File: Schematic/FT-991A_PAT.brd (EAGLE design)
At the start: 44.6 x 59.8 mm, 50 parts, among them Q10 PE4259, Q2 MC78L09ABDR2GOSCT, Q3 SN74AHC-OR, Q4 PE4259, Q5 NCP553, Q6 PE4259, Q7 J310, Q8 5086, Q9 PE4259, X1 IF_IN, X2 SCP_OUT, X3 SDR_OUT

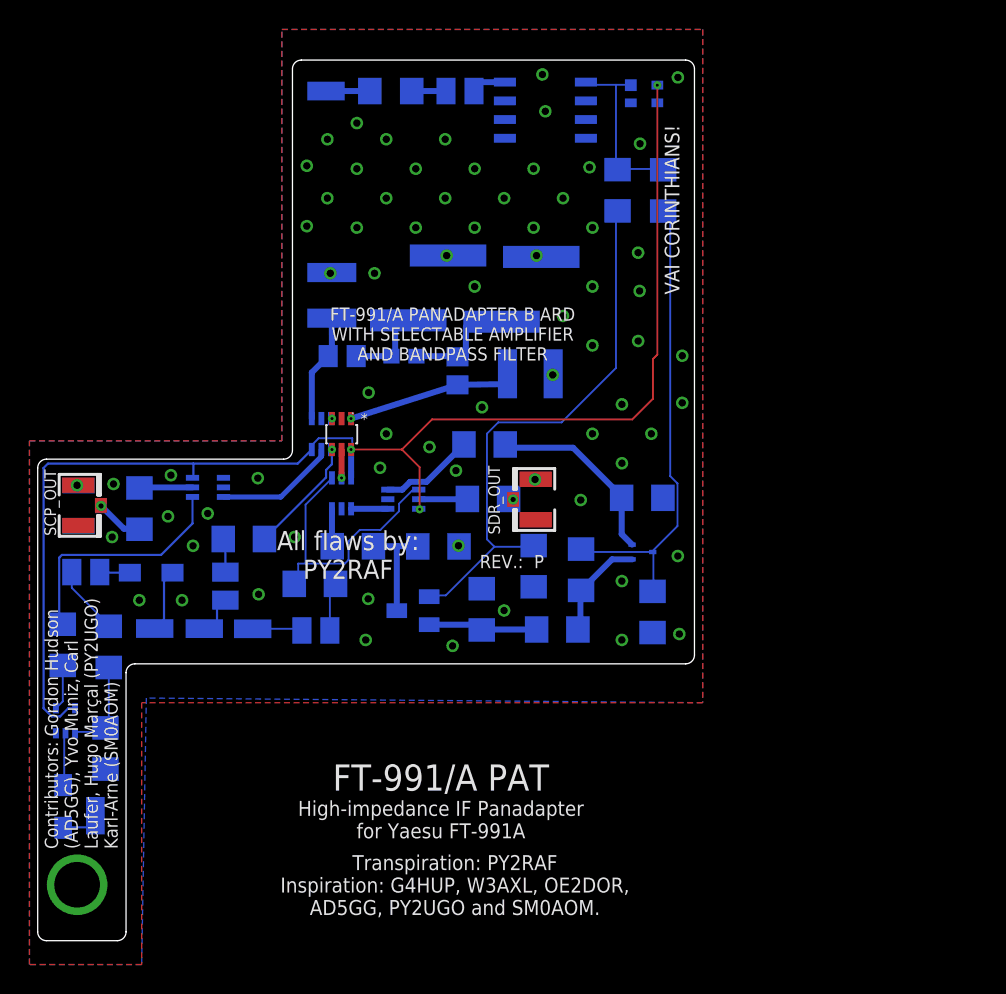
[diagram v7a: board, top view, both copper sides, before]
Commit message: Added test points
Added test points for voltage and RF switch lines.
Updated board, schematics and gerbers to reflect the change.
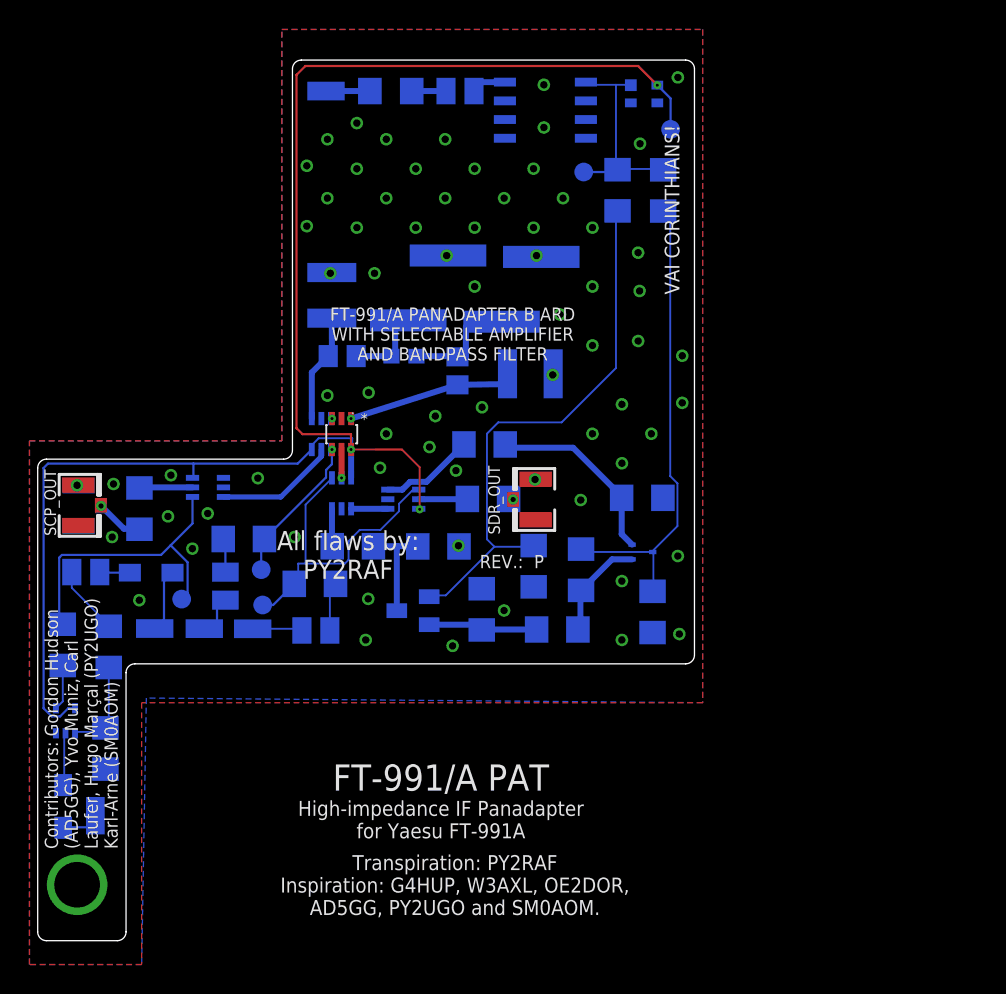
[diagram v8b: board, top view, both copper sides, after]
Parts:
- added TP1, TP2, TP3, TP4: TPB1,27, testpad:B1,27
- added TP5: BPF, testpad:B1,27
- C3, C8: value 62pF -> 56pF
- Q1: value (none) -> PE4259
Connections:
- net N$19: now also TP3.TP
- net N$40: now also TP4.TP
- net N$46: now also TP5.TP
- net VCC: now also TP1.TP
- net VDD: now also TP2.TP
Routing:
- net VDD: track 92.6 -> 110.3 mm
- net N$19: track 16.4 -> 20.7 mm
- net N$40: track 19.4 -> 22.3 mm
- net VCC: track 12.1 -> 14.5 mm
- net N$46: track 8.05 -> 10.2 mm
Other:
- board text added: "3V"
- board text added: "9V"
- board text added: "B"
- board text added: "D"
- board text added: "P"
